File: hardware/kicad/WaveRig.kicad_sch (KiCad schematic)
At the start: 0 parts

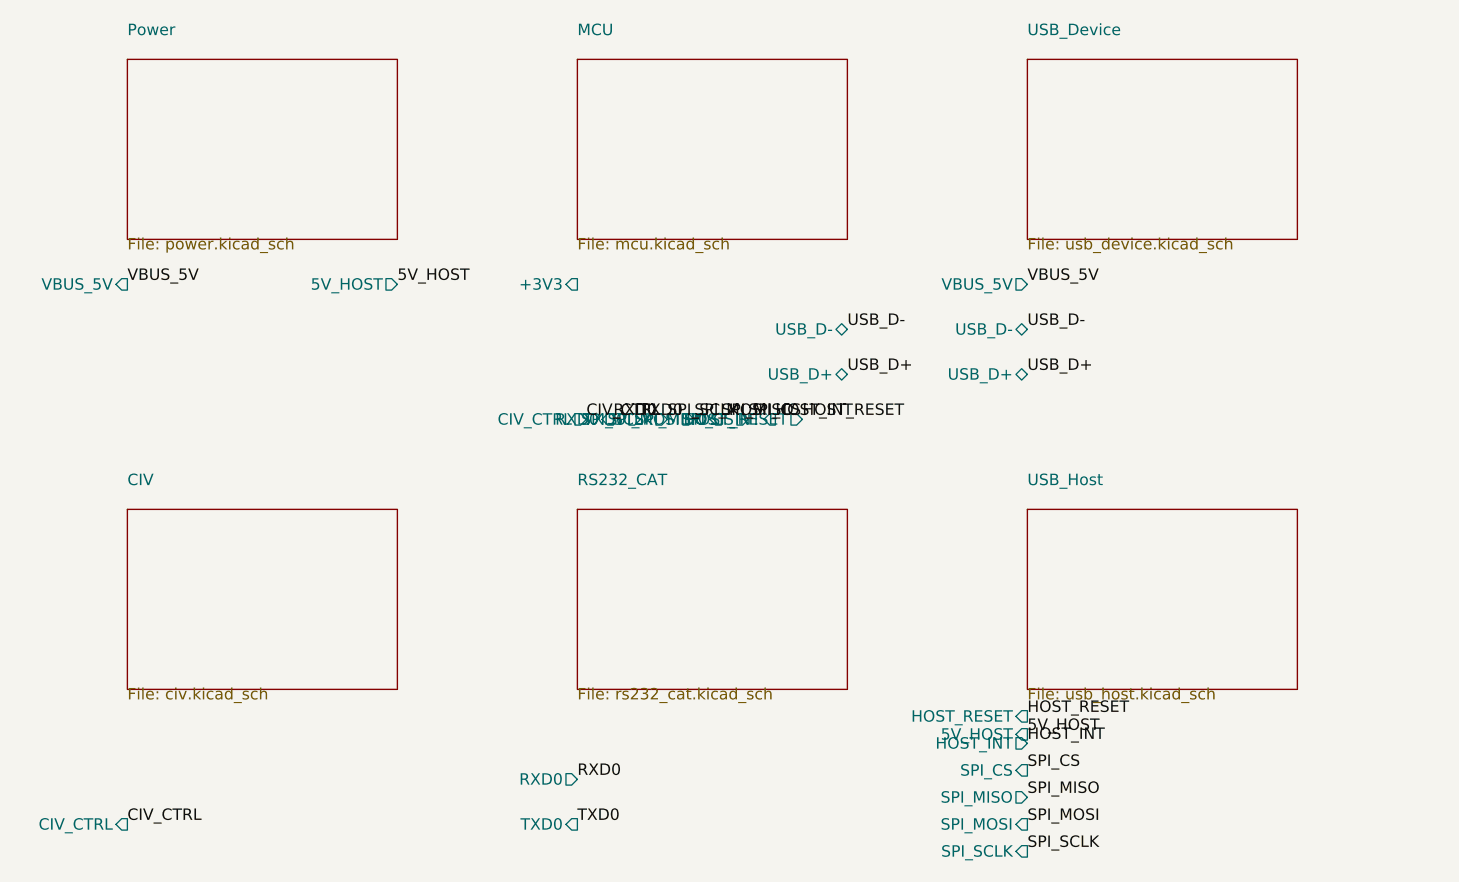
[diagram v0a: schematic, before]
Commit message: fix: repair schematic connectivity, real MAX3421E pinout, footprint assignment
- Root sheet pins were placed outside the sheet boxes, so no cross-sheet
  net (IO5->CI-V, USB D+/D-, SPI, VBUS_5V, 5V_HOST) was actually connected.
  Rebuilt pins on the sheet borders with wire stubs + labels.
- MCU: SW1/SW2 pin 2 carried both GND and EN/BOOT0 (short to ground);
  GND moved to pin 1. Unused ESP32 GPIOs marked no-connect.
- USB_Host rebuilt around the real MAX3421E TQFN-32 pinout (datasheet
  19-3953): 33 ohm D+/D- series resistors, 1uF VCC/VBCOMP, 0.1uF VL.
- J1 now AudioJack3 (T/R/S) with CUI SJ1-3523N footprint; Q1 is a real
  2N7000 (TO-92).
- PWR_FLAGs added; ERC (raw kicad-cli) has 0 errors.
- Board outline 65x45 mm, 54 footprints assigned and written to symbol
  Footprint fields, netlist applied. Placement is a rough grid only; no
  routing yet.
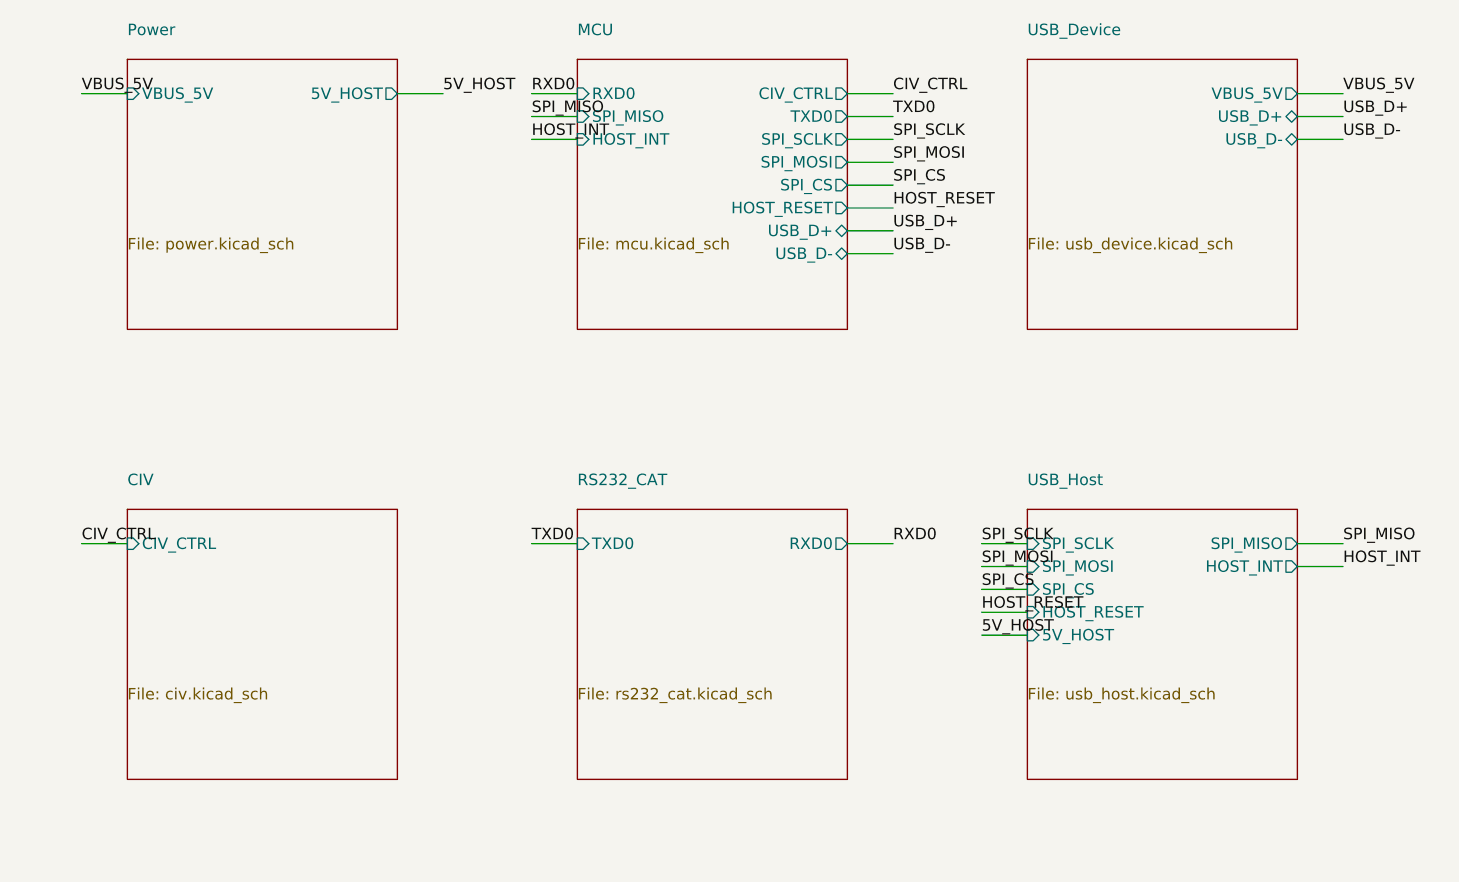
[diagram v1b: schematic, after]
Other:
- sheet MCU ports: added none; removed +3V3

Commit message: fix: datasheet audit - correct charger pinout, LDO for 3V3, DW01A/FS8205A, MAX3232, CI-V RX
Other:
- sheet CIV ports: added CIV_RX; removed none
- sheet MCU ports: added CIV_RX; removed none
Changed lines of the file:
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@@
+			)
+		)
+		(pin "CIV_RX" input
+			(at 70 51.43 180)
+			(effects
+				(font
+					(size 1.27 1.27)
+				)
+				(justify right)
 			)
 		)
@@
 			)
 		)
+		(pin "CIV_RX" output
+			(at 50 93.81 0)
+			(effects
+				(font
+					(size 1.27 1.27)
+				)
+				(justify right)
+			)
+		)
 	)
 	(sheet
@@
 	(wire
 		(pts
+			(xy 70 51.43)
+			(xy 64.92 51.43)
+		)
+		(stroke
+			(width 0)
+			(type default)
+		)
+	)
+	(label "CIV_RX"
+		(at 64.92 51.43 180)
+		(effects
+			(font
+				(size 1.27 1.27)
+			)
+			(justify left bottom)
+		)
+	)
+	(wire
+		(pts
 			(xy 100 43.81)
 			(xy 105.08 43.81)
@@
 		(effects
 			(font
+				(size 1.27 1.27)
+			)
+			(justify left bottom)
+		)
+	)
+	(wire
+		(pts
+			(xy 50 93.81)
+			(xy 55.08 93.81)
+		)
+		(stroke
+			(width 0)
+			(type default)
+		)
+	)
+	(label "CIV_RX"
+		(at 55.08 93.81 0)
+		(effects
+			(font
